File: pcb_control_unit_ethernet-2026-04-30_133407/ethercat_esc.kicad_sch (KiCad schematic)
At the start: 65 parts, among them U16 24LC512, Y2 25MHz

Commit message: WIP
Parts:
- removed C76: u1, Capacitor_SMD:C_0402_1005Metric, symbol Device:C
- removed C80: 10n, Capacitor_SMD:C_0603_1608Metric, symbol Device:C
- added C70: u1, Capacitor_SMD:C_0402_1005Metric, symbol Device:C
- C58: value 22n -> u1; footprint Capacitor_SMD:C_0603_1608Metric -> Capacitor_SMD:C_0402_1005Metric
- R64, R65, R67: footprint Resistor_SMD:R_0201_0603Metric -> Resistor_SMD:R_0402_1005Metric
- renumbered C70 to C73
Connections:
- net +3V3: now also C70.1; no longer C73.1
- net GND: now also C70.2
- net VDD33TXRX1: now also C73.1; no longer C58.1, C74.1, L9.2
- net VDD33TXRX2: now also C58.1, C74.1, L9.2
- net at C77.1, U13.1 (OSCI): now also Y2.3; no longer Y2.1
- net at C78.1, U13.2 (OSCO): now also Y2.1; no longer Y2.3
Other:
- moved on the sheet: C73, Y2

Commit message: WIP
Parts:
- R83, R84: value 2.2k -> 2k2
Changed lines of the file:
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@@
 			)
 		)
-		(property "Value" "2.2k"
+		(property "Value" "2k2"
 			(at 138.43 176.022 90)
 			(effects
@@
 			)
 		)
-		(property "Value" "2.2k"
+		(property "Value" "2k2"
 			(at 152.4 176.022 90)
 			(effects

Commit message: WIP
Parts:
- C58: value u1 -> 22n/50V
- C77, C78: value 5p6 -> 10p
- L5, L7, L8, L9: value 220R -> 220R@100M
- R67: value 4k7 -> 5k1
- R83, R84: value 2k2 -> 3k3
- U13: value ~ -> (none)
- U16: now not fitted
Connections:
- net ETHERCAT_IRQ: now reaches U13.44 (IRQ/LATCH1)
- no-connect marks 0 -> 2

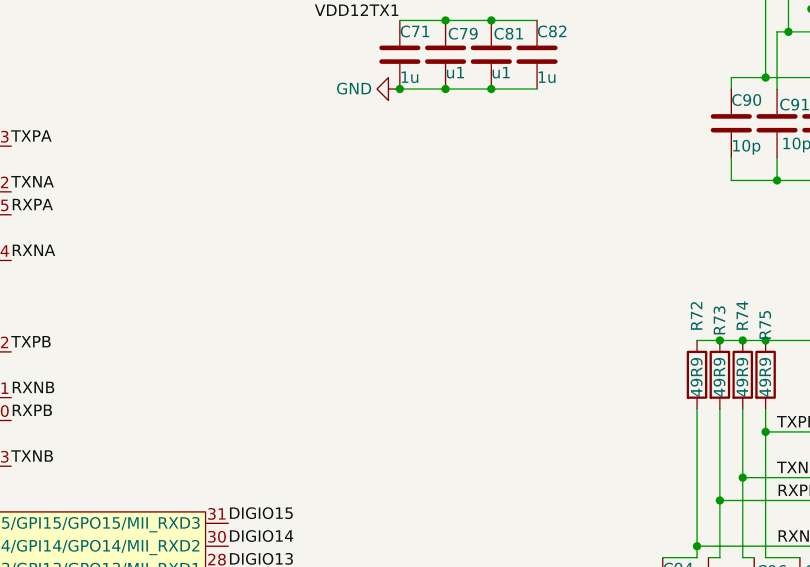
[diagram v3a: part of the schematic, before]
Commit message: Almost orderable, but: Size is too large to fit
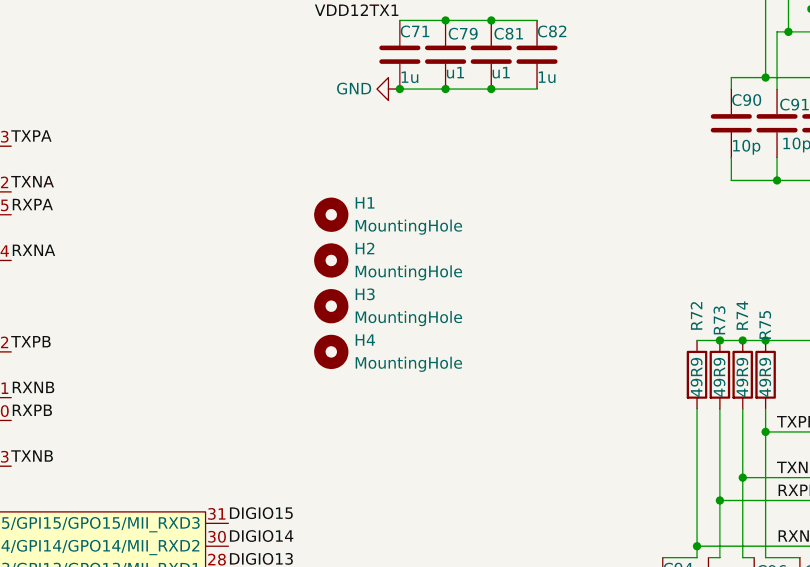
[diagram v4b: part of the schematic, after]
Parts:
- added H1, H2, H3, H4: MountingHole, MountingHole:MountingHole_4.3mm_M4_DIN965, symbol Mechanical:MountingHole
